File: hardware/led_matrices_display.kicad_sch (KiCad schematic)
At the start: 4 parts, among them U10 KWM-20882CUYB, U11 KWM-20882CUYB, U12 KWM-20882CUYB, U13 KWM-20882CUYB

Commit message: Added the values of resostors and caps that for some reason got reseted.
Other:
- title: Kitchen_Timer: LED Matrices Display -> Kitchen_Timer - LED Matrices Display
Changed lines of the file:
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@@
 	(paper "A4")
 	(title_block
-		(title "Kitchen_Timer: LED Matrices Display")
+		(title "Kitchen_Timer - LED Matrices Display")
 		(date "2025-01-26")
 		(rev "v01")
+		(comment 2 "creativecommons.org/licences/4.0/")
+		(comment 3 "Licence: CC BY 4.0")
+		(comment 4 "Author: Nicolas Perozzi")
 	)
 	(bus_entry
@@
 	(label "Mat1.DIG_0"
 		(at 71.12 49.53 0)
+		(fields_autoplaced yes)
 		(effects
 			(font
@@
 	(label "Mat1.SEG_A"
 		(at 91.44 41.91 90)
+		(fields_autoplaced yes)
 		(effects
 			(font
@@
 	)
 	(symbol
-		(lib_name "kitchen_timer-symbols_lib:LED_Matrix_KWM-2088XUYB")
 		(lib_id "kitchen_timer-symbols_lib:LED_Matrix_KWM-2088XUYB")
 		(at 135.89 99.06 180)
@@
 	)
 	(symbol
-		(lib_name "kitchen_timer-symbols_lib:LED_Matrix_KWM-2088XUYB")
 		(lib_id "kitchen_timer-symbols_lib:LED_Matrix_KWM-2088XUYB")
 		(at 135.89 63.5 0)
@@
 	)
 	(symbol
-		(lib_name "kitchen_timer-symbols_lib:LED_Matrix_KWM-2088XUYB")
 		(lib_id "kitchen_timer-symbols_lib:LED_Matrix_KWM-2088XUYB")
 		(at 109.22 99.06 0)
@@
 	)
 	(symbol
-		(lib_name "kitchen_timer-symbols_lib:LED_Matrix_KWM-2088XUYB")
 		(lib_id "kitchen_timer-symbols_lib:LED_Matrix_KWM-2088XUYB")
 		(at 109.22 63.5 0)

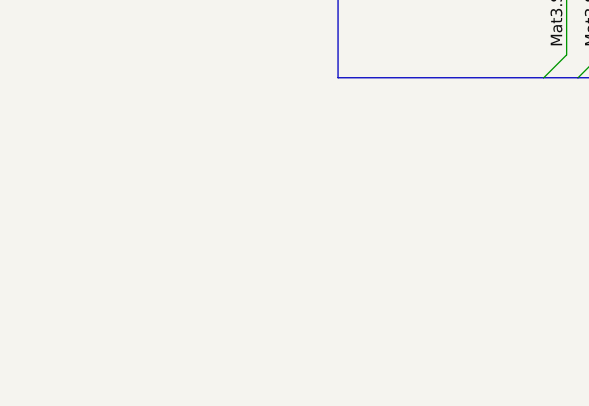
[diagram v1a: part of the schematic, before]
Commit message: Added data to the components table
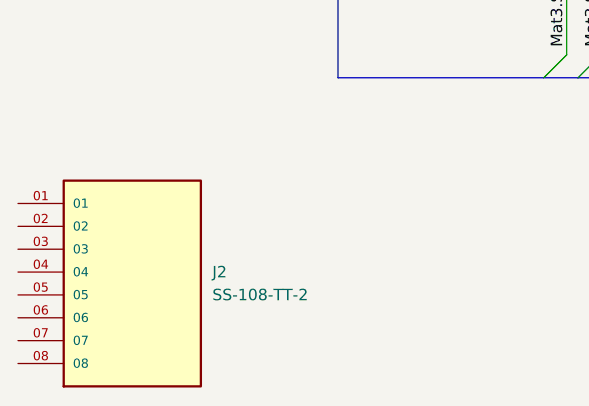
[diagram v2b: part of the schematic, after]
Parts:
- added J2: SS-108-TT-2, kitchen_timer:SAMTEC_SS-108-TT-2, symbol kitchen_timer-symbols_lib:SS-108-TT-2
- U10, U11, U12, U13: Package (none) -> Module; Part Num (none) -> KWM-2088CUYB; Price/unit (none) -> 75,00 kr; Supplier Link (none) -> https://www.electrokit.com/punktmatris-led-8x8-20.32mm-cc-g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

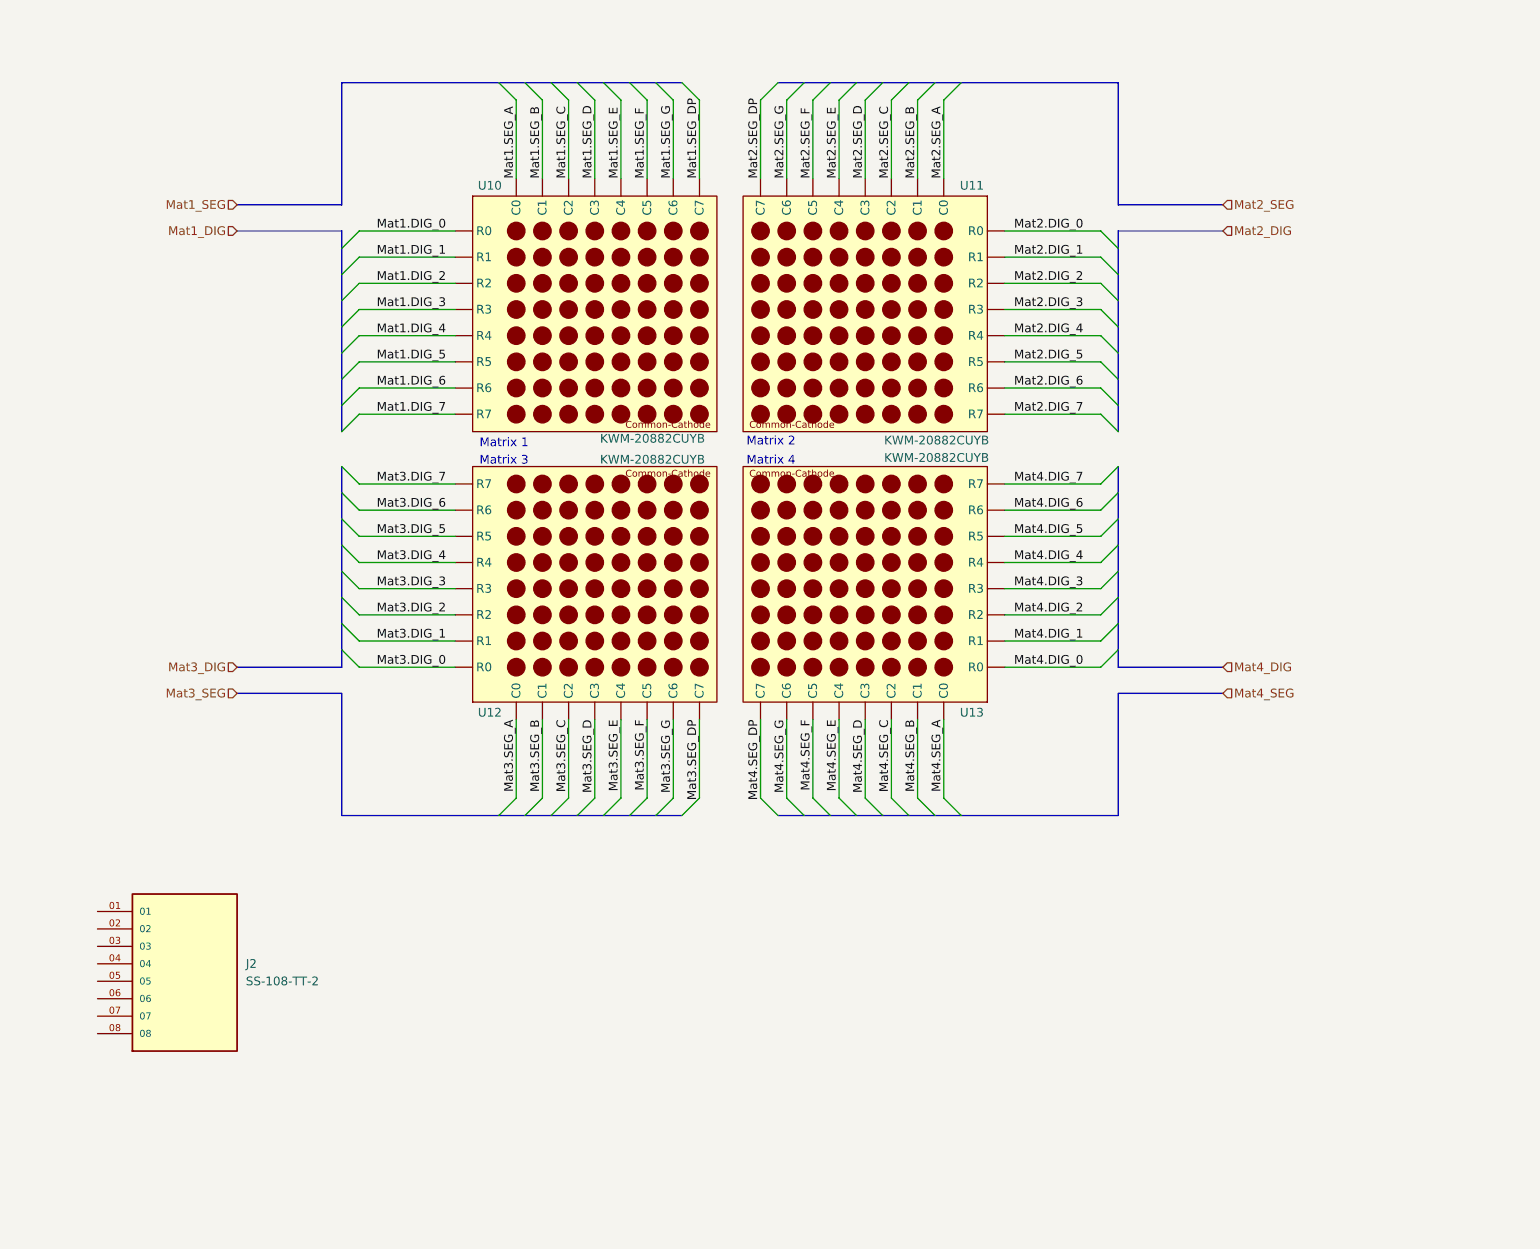
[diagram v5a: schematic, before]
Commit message: Schematic completed, commented and ready for review
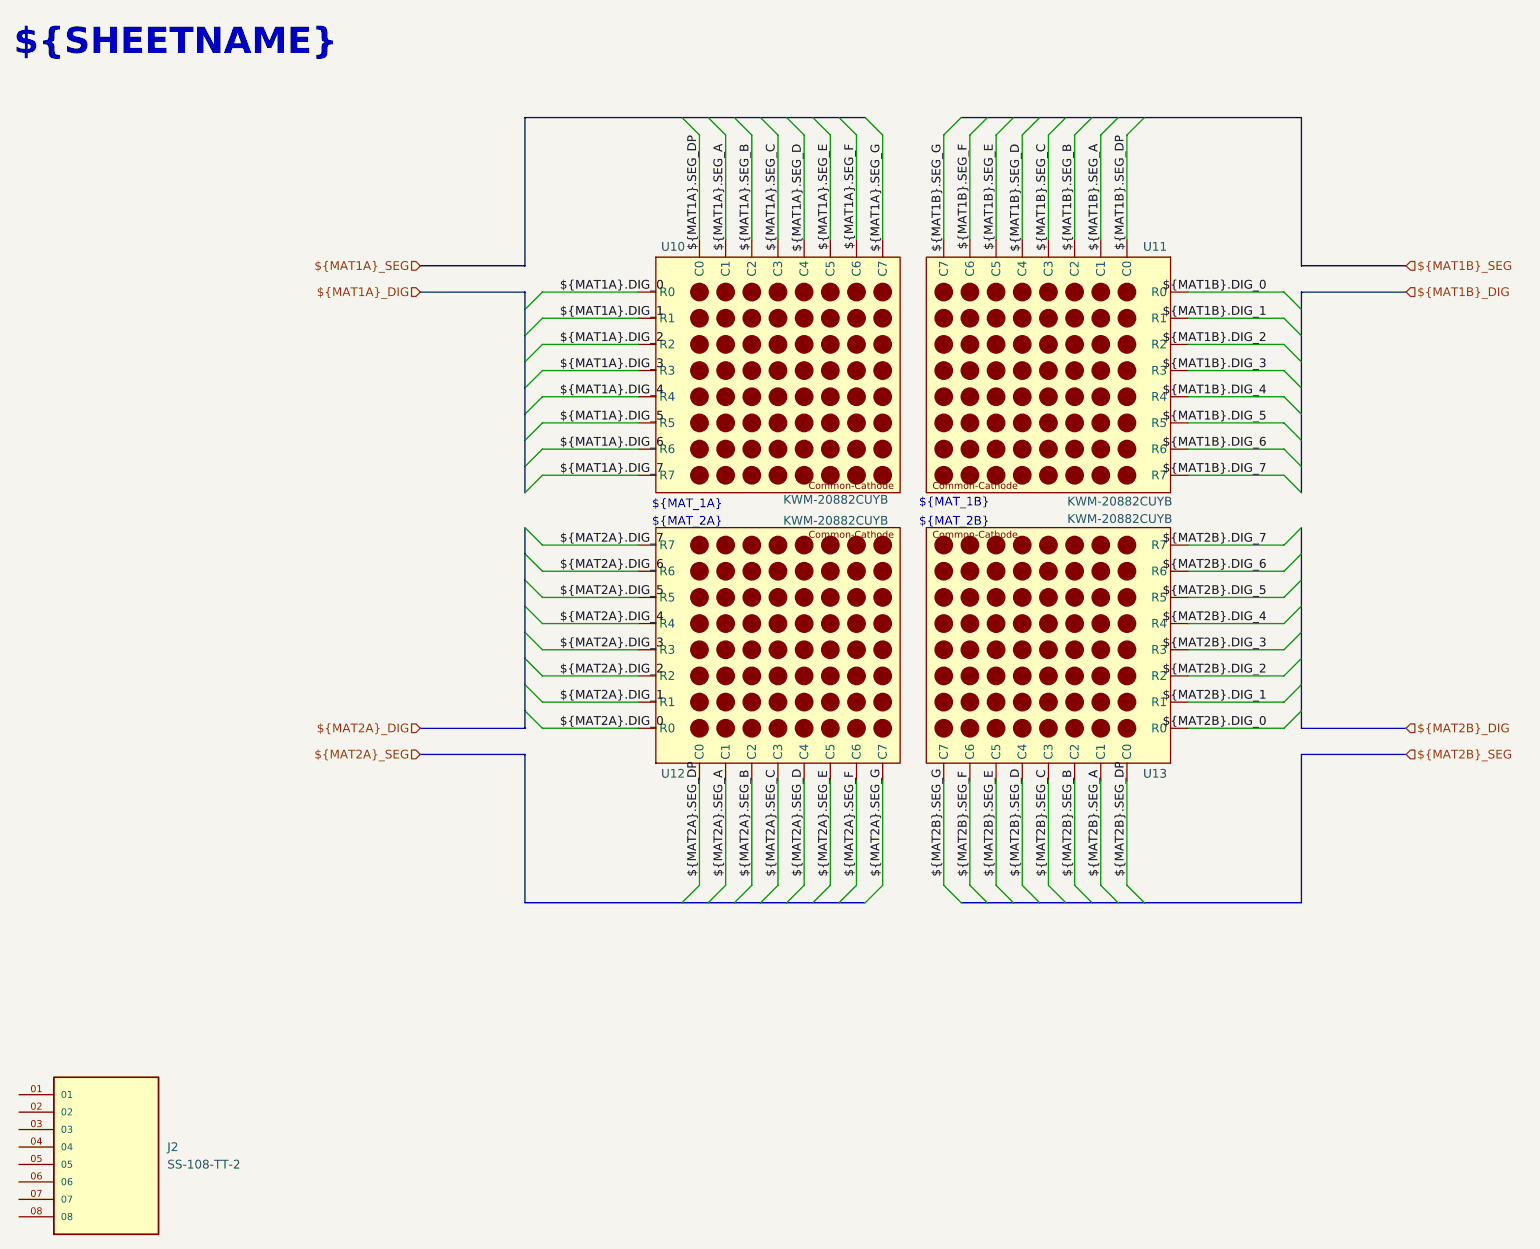
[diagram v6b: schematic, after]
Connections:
- net Mat1.DIG_1 is gone; now on net ${MAT1A}.SEG_G: U10. (C7)
- net Mat1.DIG_2 is gone; now on net ${MAT1A}.SEG_G: U10. (C7)
- net Mat1.DIG_3 is gone; now on net ${MAT1A}.SEG_G: U10. (C7)
- net Mat1.DIG_4 is gone; now on net ${MAT1A}.SEG_G: U10. (C7)
- net Mat1.DIG_5 is gone; now on net ${MAT1A}.SEG_G: U10. (C7)
- net Mat1.DIG_6 is gone; now on net ${MAT1A}.SEG_G: U10. (C7)
- net Mat1.DIG_7 is gone; now on net ${MAT1A}.SEG_G: U10. (C7)
- net Mat1.SEG_A is gone; now on net ${MAT1A}.SEG_G: U10. (C7)
- net Mat1.SEG_B is gone; now on net ${MAT1A}.SEG_G: U10. (C7)
- net Mat1.SEG_C is gone; now on net ${MAT1A}.SEG_G: U10. (C7)
- net Mat1.SEG_D is gone; now on net ${MAT1A}.SEG_G: U10. (C7)
- net Mat1.SEG_DP is gone; now on net ${MAT1A}.SEG_G: U10. (C7)
- net Mat1.SEG_E is gone; now on net ${MAT1A}.SEG_G: U10. (C7)
- net Mat1.SEG_F is gone; now on net ${MAT1A}.SEG_G: U10. (C7)
- net Mat1.SEG_G is gone; now on net ${MAT1A}.SEG_G: U10. (C7)
- net Mat2.DIG_1 is gone; now on net ${MAT1B}.SEG_G: U11. (C7)
- net Mat2.DIG_2 is gone; now on net ${MAT1B}.SEG_G: U11. (C7)
- net Mat2.DIG_3 is gone; now on net ${MAT1B}.SEG_G: U11. (C7)
- net Mat2.DIG_4 is gone; now on net ${MAT1B}.SEG_G: U11. (C7)
- net Mat2.DIG_5 is gone; now on net ${MAT1B}.SEG_G: U11. (C7)
- net Mat2.DIG_6 is gone; now on net ${MAT1B}.SEG_G: U11. (C7)
- net Mat2.DIG_7 is gone; now on net ${MAT1B}.SEG_G: U11. (C7)
- net Mat2.SEG_A is gone; now on net ${MAT1B}.SEG_G: U11. (C7)
- net Mat2.SEG_B is gone; now on net ${MAT1B}.SEG_G: U11. (C7)
- net Mat2.SEG_C is gone; now on net ${MAT1B}.SEG_G: U11. (C7)
- net Mat2.SEG_D is gone; now on net ${MAT1B}.SEG_G: U11. (C7)
- net Mat2.SEG_DP is gone; now on net ${MAT1B}.SEG_G: U11. (C7)
- net Mat2.SEG_E is gone; now on net ${MAT1B}.SEG_G: U11. (C7)
- net Mat2.SEG_F is gone; now on net ${MAT1B}.SEG_G: U11. (C7)
- net Mat2.SEG_G is gone; now on net ${MAT1B}.SEG_G: U11. (C7)
- net Mat3.DIG_1 is gone; now on net ${MAT2A}.SEG_G: U12. (C7)
- net Mat3.DIG_2 is gone; now on net ${MAT2A}.SEG_G: U12. (C7)
- net Mat3.DIG_3 is gone; now on net ${MAT2A}.SEG_G: U12. (C7)
- net Mat3.DIG_4 is gone; now on net ${MAT2A}.SEG_G: U12. (C7)
- net Mat3.DIG_5 is gone; now on net ${MAT2A}.SEG_G: U12. (C7)
- net Mat3.DIG_6 is gone; now on net ${MAT2A}.SEG_G: U12. (C7)
- net Mat3.DIG_7 is gone; now on net ${MAT2A}.SEG_G: U12. (C7)
- net Mat3.SEG_A is gone; now on net ${MAT2A}.SEG_G: U12. (C7)
- net Mat3.SEG_B is gone; now on net ${MAT2A}.SEG_G: U12. (C7)
- net Mat3.SEG_C is gone; now on net ${MAT2A}.SEG_G: U12. (C7)
- net Mat3.SEG_D is gone; now on net ${MAT2A}.SEG_G: U12. (C7)
- net Mat3.SEG_DP is gone; now on net ${MAT2A}.SEG_G: U12. (C7)
- net Mat3.SEG_E is gone; now on net ${MAT2A}.SEG_G: U12. (C7)
- net Mat3.SEG_F is gone; now on net ${MAT2A}.SEG_G: U12. (C7)
- net Mat3.SEG_G is gone; now on net ${MAT2A}.SEG_G: U12. (C7)
- net Mat4.DIG_1 is gone; now on net ${MAT2B}.SEG_G: U13. (C7)
- net Mat4.DIG_2 is gone; now on net ${MAT2B}.SEG_G: U13. (C7)
- net Mat4.DIG_3 is gone; now on net ${MAT2B}.SEG_G: U13. (C7)
- net Mat4.DIG_4 is gone; now on net ${MAT2B}.SEG_G: U13. (C7)
- net Mat4.DIG_5 is gone; now on net ${MAT2B}.SEG_G: U13. (C7)
- net Mat4.DIG_6 is gone; now on net ${MAT2B}.SEG_G: U13. (C7)
- net Mat4.DIG_7 is gone; now on net ${MAT2B}.SEG_G: U13. (C7)
- net Mat4.SEG_A is gone; now on net ${MAT2B}.SEG_G: U13. (C7)
- net Mat4.SEG_B is gone; now on net ${MAT2B}.SEG_G: U13. (C7)
- net Mat4.SEG_C is gone; now on net ${MAT2B}.SEG_G: U13. (C7)
- net Mat4.SEG_D is gone; now on net ${MAT2B}.SEG_G: U13. (C7)
- net Mat4.SEG_DP is gone; now on net ${MAT2B}.SEG_G: U13. (C7)
- net Mat4.SEG_E is gone; now on net ${MAT2B}.SEG_G: U13. (C7)
- net Mat4.SEG_F is gone; now on net ${MAT2B}.SEG_G: U13. (C7)
- net Mat4.SEG_G is gone; now on net ${MAT2B}.SEG_G: U13. (C7)
- net Mat1.DIG_0 renamed ${MAT1A}.SEG_G
- net Mat2.DIG_0 renamed ${MAT1B}.SEG_G
- net Mat3.DIG_0 renamed ${MAT2A}.SEG_G
- net Mat4.DIG_0 renamed ${MAT2B}.SEG_G
- new net ${MAT1A}.DIG_0: U10. (C7)
- new net ${MAT1A}.DIG_1: U10. (C7)
- new net ${MAT1A}.DIG_2: U10. (C7)
- new net ${MAT1A}.DIG_3: U10. (C7)
- new net ${MAT1A}.DIG_4: U10. (C7)
- new net ${MAT1A}.DIG_5: U10. (C7)
- new net ${MAT1A}.DIG_6: U10. (C7)
- new net ${MAT1A}.DIG_7: U10. (C7)
- new net ${MAT1A}.SEG_A: U10. (C7)
- new net ${MAT1A}.SEG_B: U10. (C7)
- new net ${MAT1A}.SEG_C: U10. (C7)
- new net ${MAT1A}.SEG_D: U10. (C7)
- new net ${MAT1A}.SEG_DP: U10. (C7)
- new net ${MAT1A}.SEG_E: U10. (C7)
- new net ${MAT1A}.SEG_F: U10. (C7)
- new net ${MAT1B}.DIG_0: U11. (C7)
- new net ${MAT1B}.DIG_1: U11. (C7)
- new net ${MAT1B}.DIG_2: U11. (C7)
- new net ${MAT1B}.DIG_3: U11. (C7)
- new net ${MAT1B}.DIG_4: U11. (C7)
- new net ${MAT1B}.DIG_5: U11. (C7)
- new net ${MAT1B}.DIG_6: U11. (C7)
- new net ${MAT1B}.DIG_7: U11. (C7)
- new net ${MAT1B}.SEG_A: U11. (C7)
- new net ${MAT1B}.SEG_B: U11. (C7)
- new net ${MAT1B}.SEG_C: U11. (C7)
- new net ${MAT1B}.SEG_D: U11. (C7)
- new net ${MAT1B}.SEG_DP: U11. (C7)
- new net ${MAT1B}.SEG_E: U11. (C7)
- new net ${MAT1B}.SEG_F: U11. (C7)
- new net ${MAT2A}.DIG_0: U12. (C7)
- new net ${MAT2A}.DIG_1: U12. (C7)
- new net ${MAT2A}.DIG_2: U12. (C7)
- new net ${MAT2A}.DIG_3: U12. (C7)
- new net ${MAT2A}.DIG_4: U12. (C7)
- new net ${MAT2A}.DIG_5: U12. (C7)
- new net ${MAT2A}.DIG_6: U12. (C7)
- new net ${MAT2A}.DIG_7: U12. (C7)
- new net ${MAT2A}.SEG_A: U12. (C7)
- new net ${MAT2A}.SEG_B: U12. (C7)
- new net ${MAT2A}.SEG_C: U12. (C7)
- new net ${MAT2A}.SEG_D: U12. (C7)
- new net ${MAT2A}.SEG_DP: U12. (C7)
- new net ${MAT2A}.SEG_E: U12. (C7)
- new net ${MAT2A}.SEG_F: U12. (C7)
- new net ${MAT2B}.DIG_0: U13. (C7)
- new net ${MAT2B}.DIG_1: U13. (C7)
- new net ${MAT2B}.DIG_2: U13. (C7)
- new net ${MAT2B}.DIG_3: U13. (C7)
- new net ${MAT2B}.DIG_4: U13. (C7)
- new net ${MAT2B}.DIG_5: U13. (C7)
- new net ${MAT2B}.DIG_6: U13. (C7)
- new net ${MAT2B}.DIG_7: U13. (C7)
- new net ${MAT2B}.SEG_A: U13. (C7)
- new net ${MAT2B}.SEG_B: U13. (C7)
- new net ${MAT2B}.SEG_C: U13. (C7)
- new net ${MAT2B}.SEG_D: U13. (C7)
- new net ${MAT2B}.SEG_DP: U13. (C7)
- new net ${MAT2B}.SEG_E: U13. (C7)
- new net ${MAT2B}.SEG_F: U13. (C7)
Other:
- note added: "${MAT_1A}"
- note added: "${MAT_1B}"
- note added: "${MAT_2A}"
- note added: "${MAT_2B}"
- note added: "${SHEETNAME}"
- note removed: "Matrix 1"
- note removed: "Matrix 2"
- note removed: "Matrix 3"
- note removed: "Matrix 4"
- title: Kitchen_Timer - LED Matrices Display -> Kitchen_Timer - ${SHEETNAME}
- moved on the sheet: J2, U10, U11, U12, U13
